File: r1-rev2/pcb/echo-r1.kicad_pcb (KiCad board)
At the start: 6 copper layers, 140 x 120.6 mm, 143 parts, among them J1 TYPE-C-31-M-12, J2 TF-115, J3 HP_3.5mm, J4 LO_3.5mm, J5 GT-BTP30003-xxxA-16A, J6 AFC07-S30ECA-00, Q1 AO3401A, Q2 AO3401A, Q3 AO3401A, Q4 AO3401A, Q5 AO3401A, SW1 A, SW10 SELECT, SW11 VOL+, SW12 VOL-, SW13 POWER, SW14 HOLD, SW2 B, SW3 X, SW4 Y, SW5 DPAD↑, SW6 DPAD↓, SW7 DPAD←, SW8 DPAD→, SW9 START, U1 STM32H7R3Z8Jx, U10 USBLC6-2SC6, U11 TPAZ1143-04F, U12 TPAZ1143-04F, U15 TPAZ1143-04F, U16 TPAZ1143-04F, U2 W958D8NBYA5I, U3 TLV320AIC3104, U4 LM66100DCK, U5 TPS62A01DRLR, U6 TPS62A01DRLR, U7 AP2125K-3.0, U8 AP2125K-3.0, U9 TP4057, Y1 SC-32S32.768kHz20PPM12.5pF, Y2 XTM32024000JT00351001

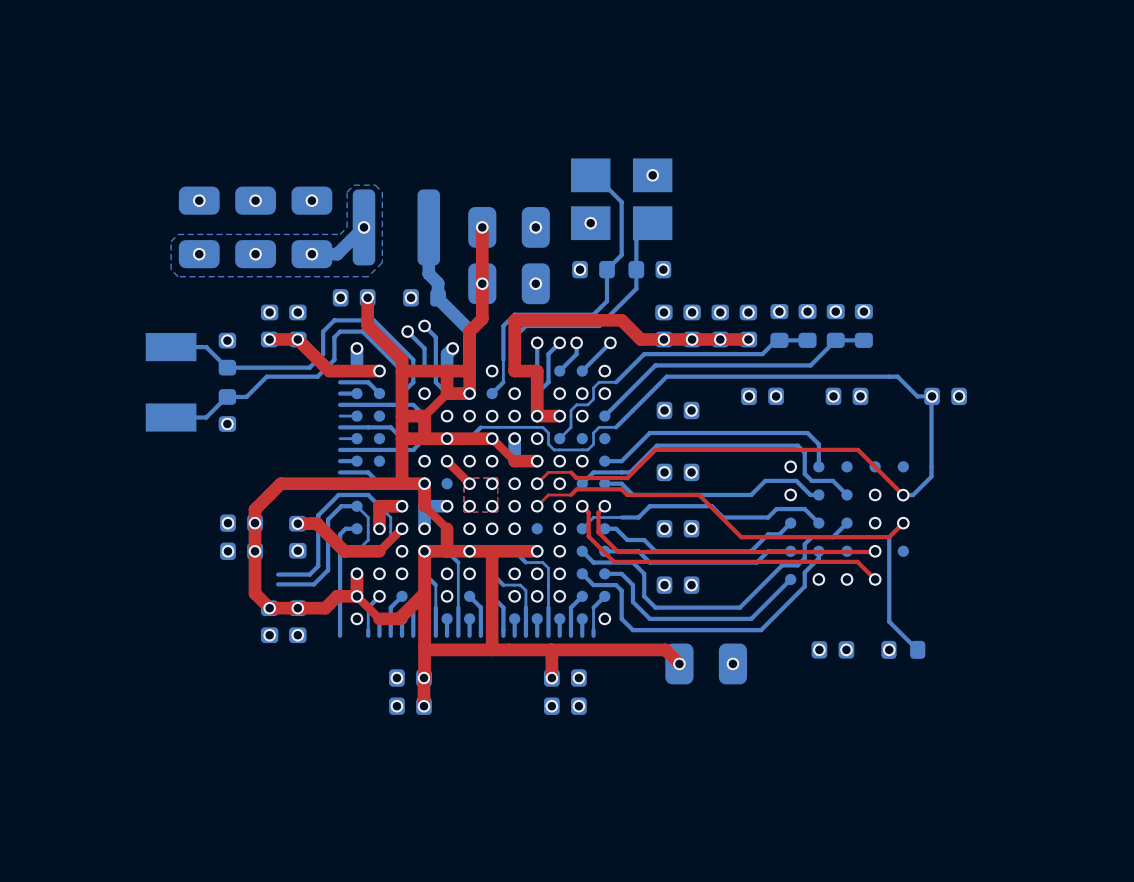
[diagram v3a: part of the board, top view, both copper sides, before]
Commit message: R1-Rev2: update pin assignment; add internal memory card slot
- Removed old H743 and H7R3 LQFP144 pin assignment sheets
- Updated pin assignments to make room for a 2nd card slot
- Added internal memory card slot
- Unassigned GPIOs and removed WIP routing
- Fixed net tie reference designators
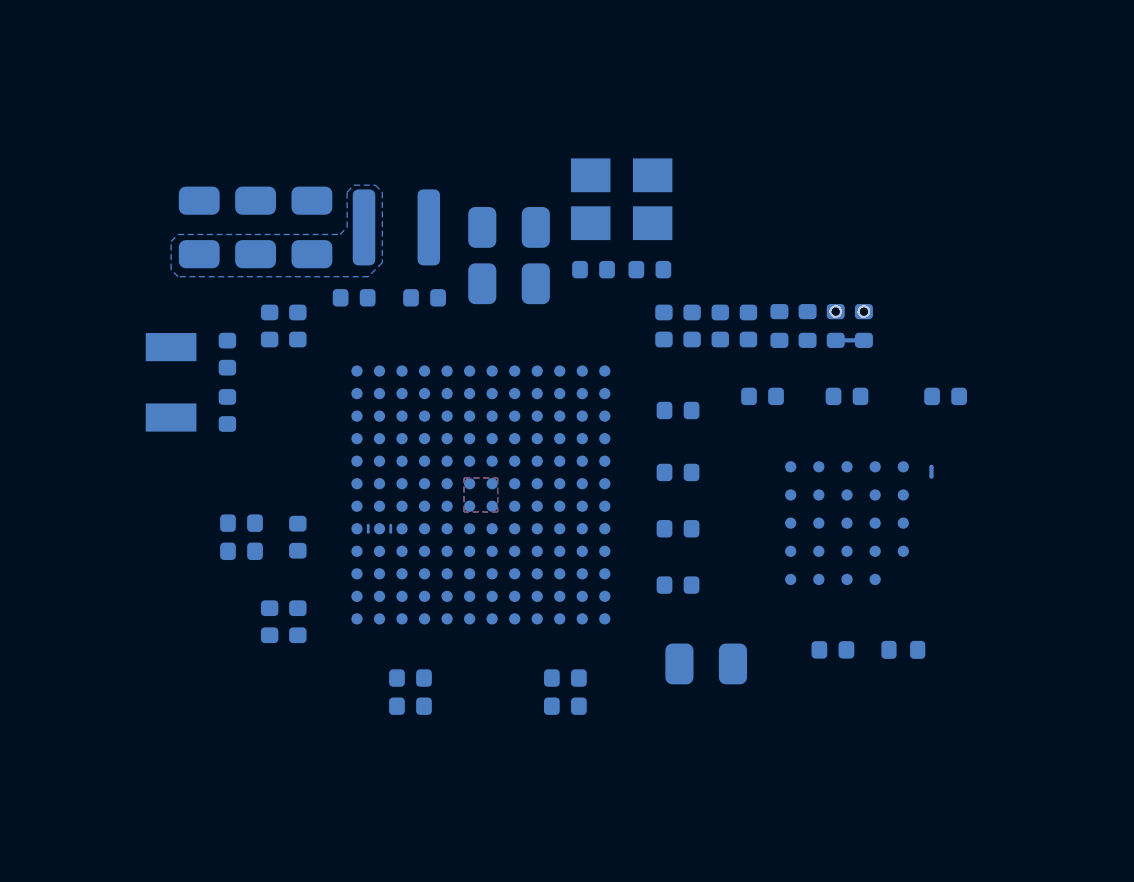
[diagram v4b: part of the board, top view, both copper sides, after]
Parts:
- renumbered NT11 to NT1, NT1 to NT2, NT8 to NT3, NT9 to NT4, NT6 to NT5, NT7 to NT6
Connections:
- net /sdmmc.clk renamed /sdmmc_ext.clk
- net /sdmmc.cmd renamed /sdmmc_ext.cmd
- net /sdmmc.d0 renamed /sdmmc_ext.d0
- net /sdmmc.d1 renamed /sdmmc_ext.d1
- net /sdmmc.d2 renamed /sdmmc_ext.d2
- net /sdmmc.d3 renamed /sdmmc_ext.d3
- net /sdmmc_pwr renamed /sdmmc_ext_pwr
- J2 pad 9: /sdmmc_detect -> /sdmmc_ext_detect
- Q2 pad 1: /sdmmc_pwr_en -> /sdmmc_ext_pwr_en
- R14 pad 2: /sdmmc_pwr_en -> /sdmmc_ext_pwr_en
- U1 pad A3: /sdmmc_pwr_en -> /uart_tx
- U1 pad A4: /sdmmc_detect -> unconnected-(U1-PB5-PadA4)
- U1 pad A5: /button_vol+ -> /sdmmc_int.cmd
- U1 pad A8: /button_vol- -> unconnected-(U1-PM9-PadA8)
- U1 pad B10: /codec_dvdd_en -> unconnected-(U1-PM2-PadB10)
- U1 pad B11: /codec_reset -> unconnected-(U1-PM3-PadB11)
- U1 pad B12: /lcd_reset -> unconnected-(U1-PD4-PadB12)
- U1 pad B5: unconnected-(U1-PB3(JTDO-PadB5) -> /sdmmc_int.d2
- U1 pad C10: /codec_avdd_en -> unconnected-(U1-PM1-PadC10)
- U1 pad C3: unconnected-(U1-PB9-PadC3) -> /codec_ctl.sda
- U1 pad C5: unconnected-(U1-PB4(NJTRST)-PadC5) -> /sdmmc_int.d3
- U1 pad C6: unconnected-(U1-PD6-PadC6) -> /sdmmc_int.clk
- U1 pad D12: /chg_enable -> unconnected-(U1-PA15(JTDI)-PadD12)
- U1 pad D4: /codec_ctl.sda -> /uart_rx
- U1 pad G3: /button_hold -> unconnected-(U1-PC0-PadG3)
- U1 pad H10: /button_left -> unconnected-(U1-PB12-PadH10)
- U1 pad H12: /chg_charging -> unconnected-(U1-PC6-PadH12)
- U1 pad H9: /uart_tx -> /sdmmc_int.d0
- U1 pad J10: /button_up -> unconnected-(U1-PB10-PadJ10)
- U1 pad J11: /button_right -> unconnected-(U1-PB13-PadJ11)
- U1 pad J12: /uart_rx -> /sdmmc_int.d1
- U1 pad J4: /button_x -> unconnected-(U1-PA5-PadJ4)
- U1 pad J6: /xspi_reset -> unconnected-(U1-PO1-PadJ6)
- U1 pad K11: /button_power -> unconnected-(U1-PD12-PadK11)
- U1 pad K12: /button_down -> unconnected-(U1-PB11-PadK12)
- U1 pad K2: /button_a -> unconnected-(U1-PA3-PadK2)
- U1 pad L11: /button_select -> unconnected-(U1-PD11-PadL11)
- U1 pad L2: /button_b -> unconnected-(U1-PA4-PadL2)
- U1 pad L3: /lo_detect -> unconnected-(U1-PC4-PadL3)
- U1 pad M11: /button_start -> unconnected-(U1-PD10-PadM11)
- U1 pad M2: /button_y -> unconnected-(U1-PA6-PadM2)
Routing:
- net +3V3: track 68.4 -> 0.00 mm, vias 22 -> 0
- net /vfbsmps: track 41.1 -> 0.00 mm, vias 15 -> 0
- net +1V8: track 39.5 -> 0.00 mm, vias 14 -> 0
- net /swd.nrst: track 21.3 -> 0.00 mm, vias 1 -> 0
- net /xspi.cs: track 19.3 -> 0.00 mm, vias 2 -> 0
- net +3V0_VBAT: track 17.9 -> 0.00 mm, vias 9 -> 0
- net /xspi_reset: track 15.6 -> 0.00 mm, vias 2 -> 0
- net /xspi.dqs0: track 12.2 -> 0.00 mm
- net /osc32k_out: track 12.0 -> 0.00 mm
- net /xspi.ck-: track 12.0 -> 0.00 mm, vias 2 -> 0
- net /osc24m_in: track 11.8 -> 0.00 mm
- net /xspi.d1: track 11.4 -> 0.00 mm
- net /xspi.ck+: track 11.1 -> 0.00 mm, vias 2 -> 0
- net /xspi.d2: track 11.1 -> 0.00 mm
- net /adc_vbat: track 10.8 -> 0.00 mm
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
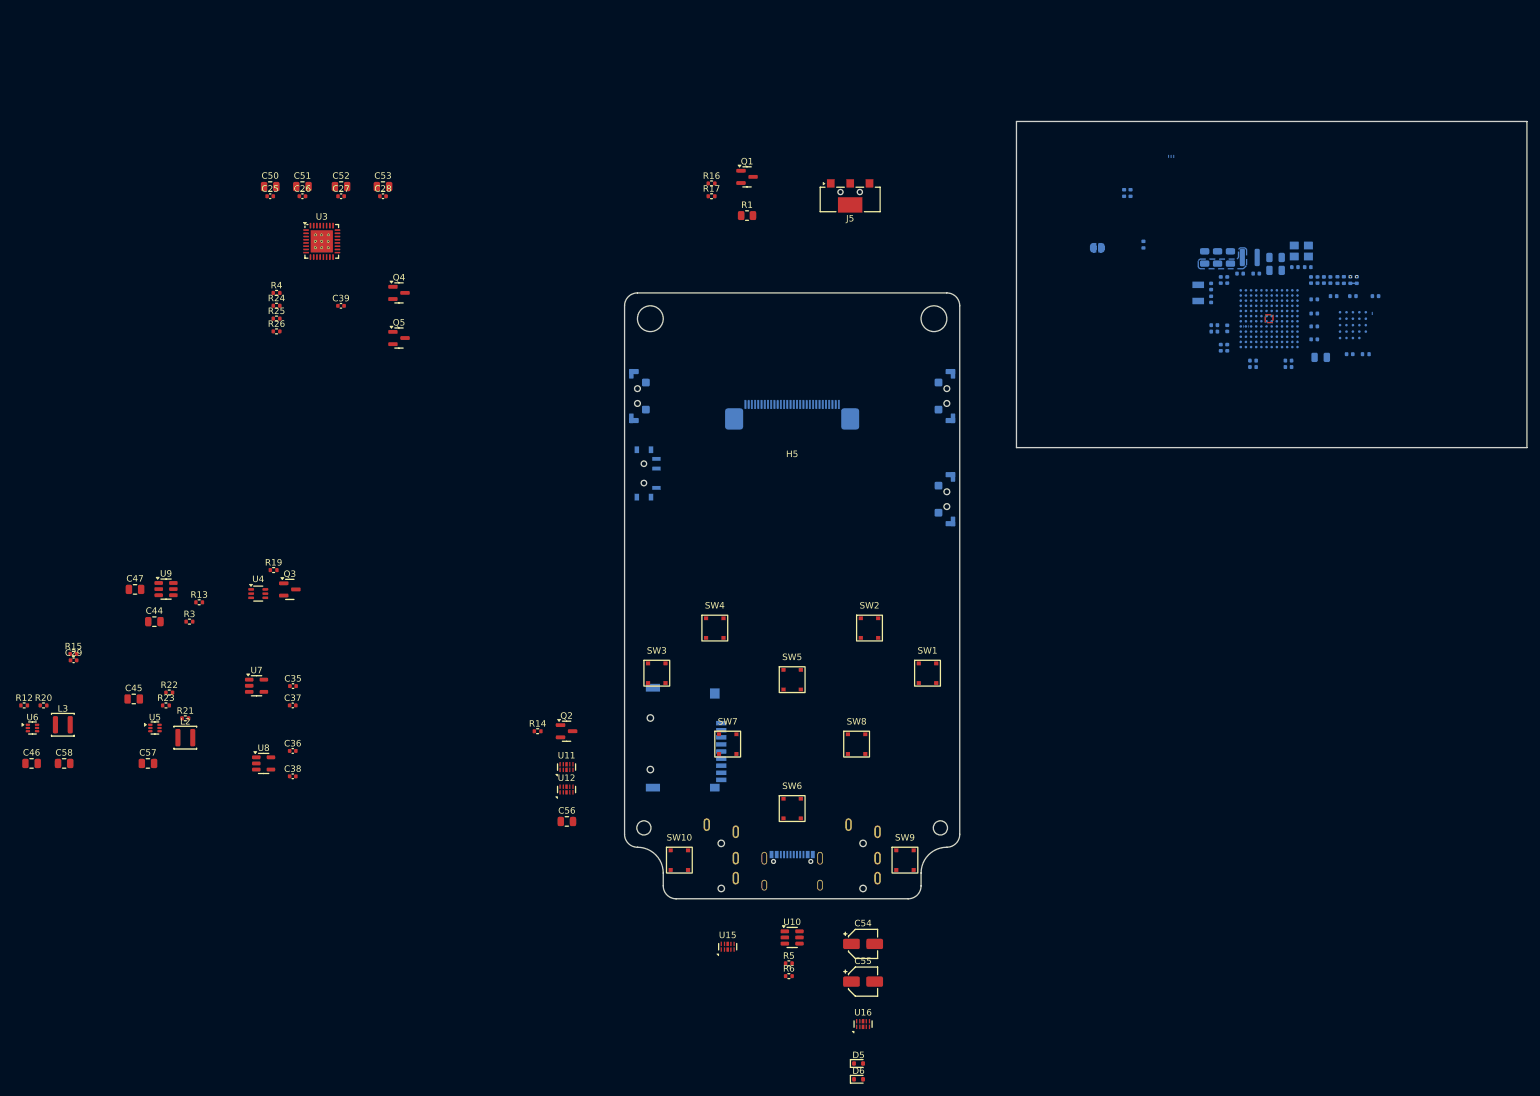
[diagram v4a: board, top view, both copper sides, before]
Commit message: R1-Rev2: add internal SD card slot footprint
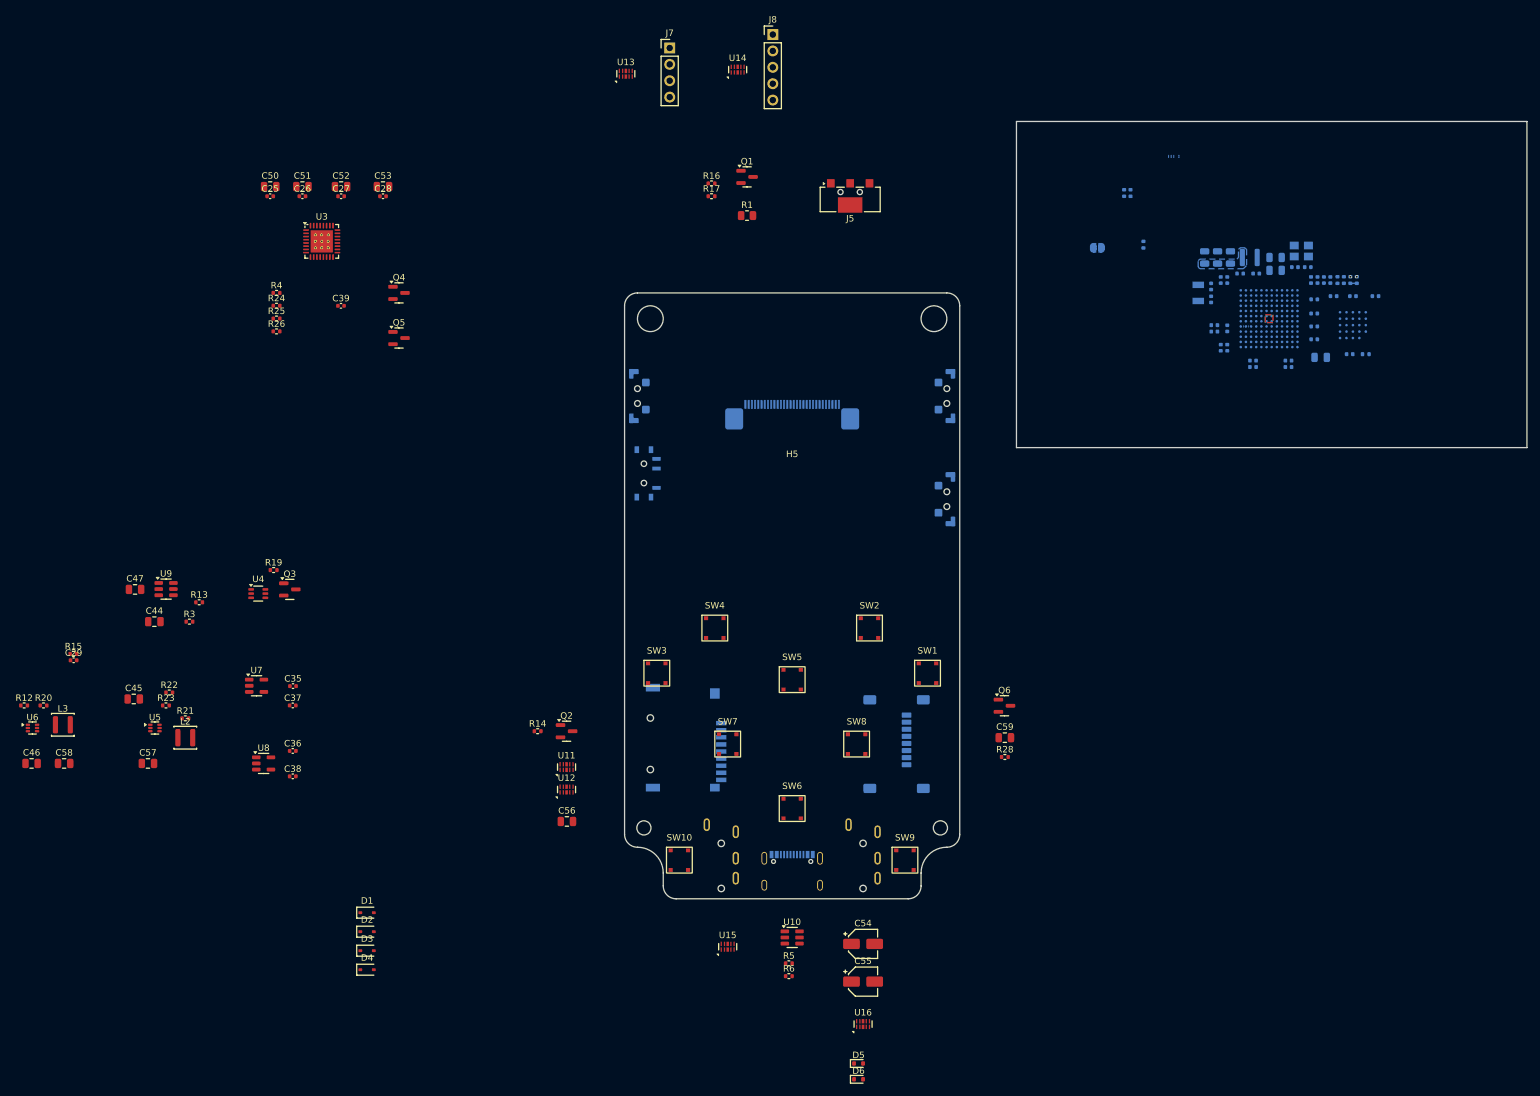
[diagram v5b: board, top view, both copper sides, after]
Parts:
- added C59: 22 µF, Capacitor_SMD:C_0805_2012Metric, F.Cu at (180.5, 127.0)
- added D1: 1N5819WS, Diode_SMD:D_SOD-323, F.Cu at (81.5, 154.2)
- added D2: 1N5819WS, Diode_SMD:D_SOD-323, F.Cu at (81.5, 157.1)
- added D3: 1N5819WS, Diode_SMD:D_SOD-323, F.Cu at (81.5, 160.1)
- added D4: 1N5819WS, Diode_SMD:D_SOD-323, F.Cu at (81.5, 163.0)
- added J7: Conn_01x04, Connector_PinHeader_2.54mm:PinHeader_1x04_P2.54mm_Vertical, F.Cu at (128.5, 20.0)
- added J8: Conn_01x05, Connector_PinHeader_2.54mm:PinHeader_1x05_P2.54mm_Vertical, F.Cu at (144.5, 17.9)
- added J9: Micro_SD_Card, echoplayer:microSD_XUNPU_TF-102-15, B.Cu at (162.5, 128.0)
- added Q6: AO3401A, Package_TO_SOT_SMD:SOT-23, F.Cu at (180.4, 122.0)
- added R28: 68 kΩ, Resistor_SMD:R_0402_1005Metric, F.Cu at (180.5, 130.0)
- added U13: TPAZ1143-04F, echoplayer:TECHPUBLIC_UDFN-10_1.0x2.5mm_P0.5mm, F.Cu at (121.7, 24.0)
- added U14: TPAZ1143-04F, echoplayer:TECHPUBLIC_UDFN-10_1.0x2.5mm_P0.5mm, F.Cu at (139.0, 23.4)
- moved NT1 38.6 mm to (207.5, 36.8)

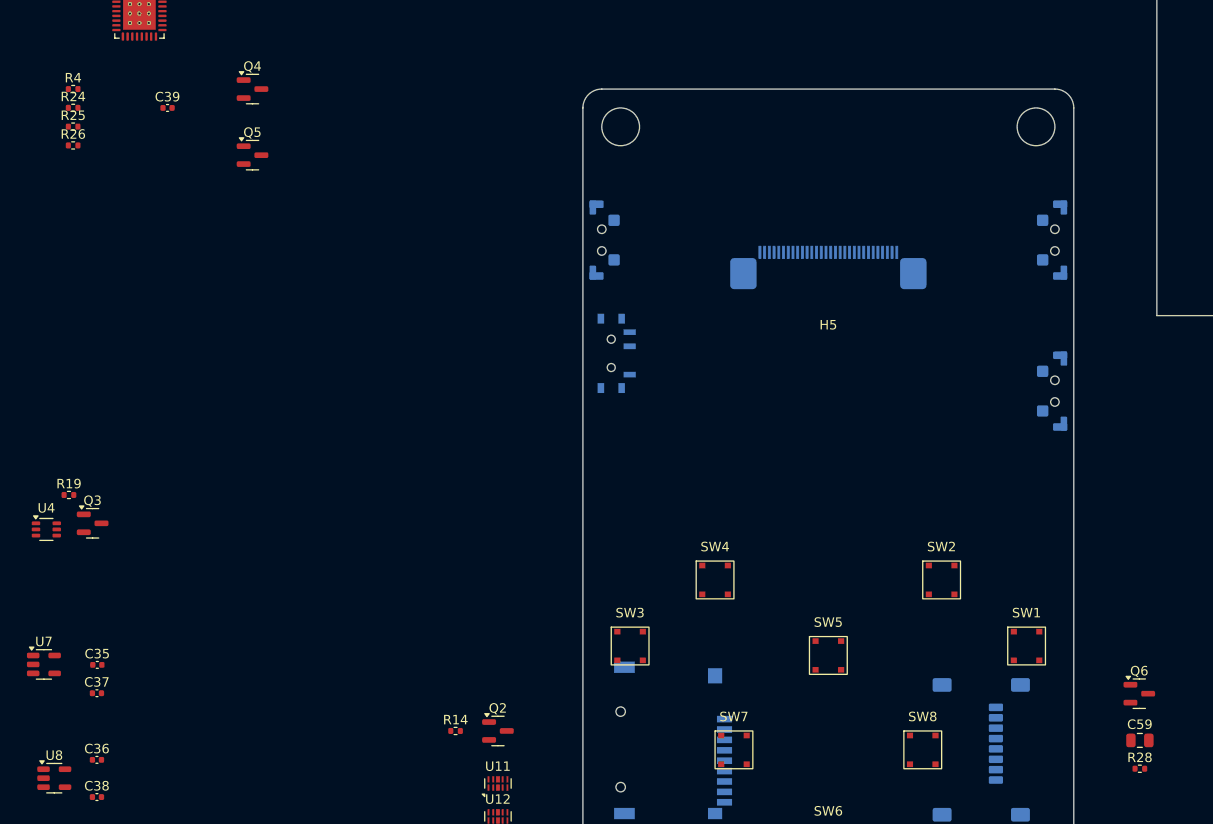
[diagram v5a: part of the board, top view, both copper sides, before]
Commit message: R1-Rev2: use LDO enable pin to control codec AVDD supply
Now that the codec has a dedicated power supply for AVDD,
the LDO's enable pin can be used for power sequencing.
This eliminates a resistor and PMOS.
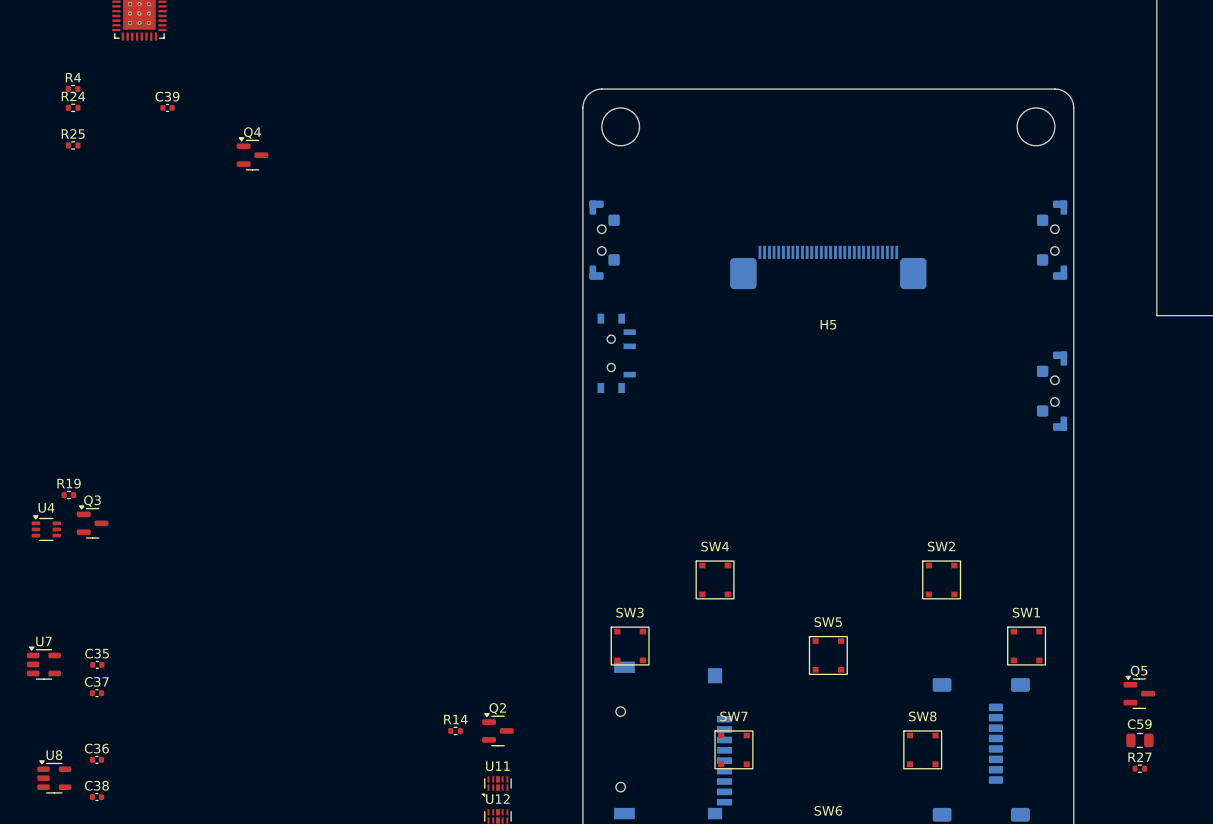
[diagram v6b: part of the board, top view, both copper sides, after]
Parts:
- removed the Q4 at (86.5, 58.0)
- removed the R25 at (67.5, 62.0)
- renumbered Q5 to Q4, Q6 to Q5, R26 to R25, R27 to R26, R28 to R27
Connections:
- U3 pad 18: /audio/avdd -> +3V0_AUDIO
- U3 pad 24: /audio/avdd -> +3V0_AUDIO
- U3 pad 25: /audio/avdd -> +3V0_AUDIO
- U8 pad 3: +3V3 -> /codec_avdd_en
